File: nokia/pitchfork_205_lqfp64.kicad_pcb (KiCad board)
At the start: 2 copper layers, 108 x 41.5 mm, 85 parts, among them IC1 STM32F2XX_64LQFP, K1 CONN_3, U1 LM3670, U2 USBCONN, U3 MCP73832-2, U4 NRF24L01+, U5 MC74VHC1G66, U6 MICROSDCARD, U7 TSV912, U8 TC75W57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

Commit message: [fix] outer rings for buttons on nokia board
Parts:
- added 1Pin_12mil_VIA: VAL**, opendous:1Pin_12mil_VIA, F.Cu at (309.3, 146.4)
- added 1Pin_12mil_VIA: VAL**, opendous:1Pin_12mil_VIA, F.Cu at (278.9, 147.7)
- added 1Pin_12mil_VIA: VAL**, opendous:1Pin_12mil_VIA, F.Cu at (279.1, 144.9)
- added 1Pin_12mil_VIA: VAL**, opendous:1Pin_12mil_VIA, F.Cu at (281.6, 143.5)
- added 1Pin_12mil_VIA: VAL**, opendous:1Pin_12mil_VIA, F.Cu at (302.0, 147.6)
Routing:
- net /usb_5v: track 117.2 -> 120.9 mm
- net /usb_dm: track 66.2 -> 66.6 mm, vias 0 -> 2
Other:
- board text added: "PITCHFORK d10011"
- board text removed: "PITCHFORK d10010"

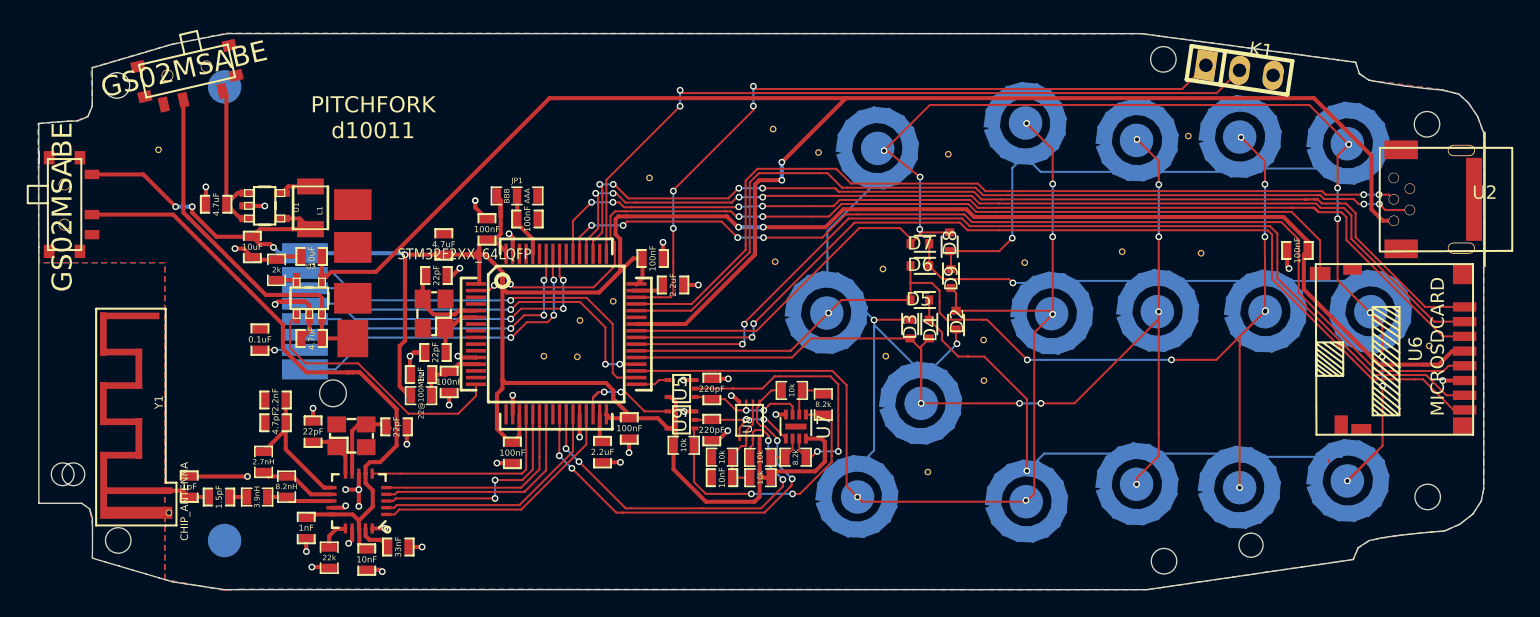
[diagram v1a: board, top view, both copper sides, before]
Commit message: [fix] lcd pinout + added R for nrf switch
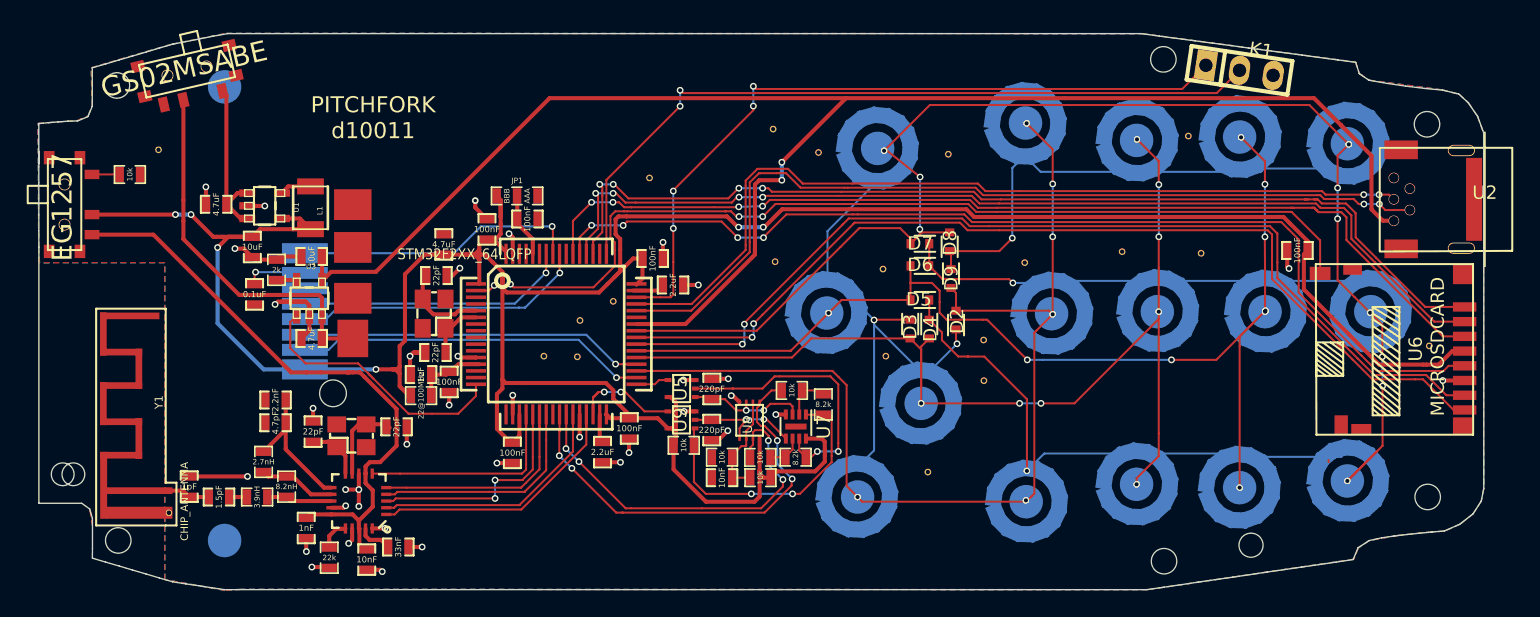
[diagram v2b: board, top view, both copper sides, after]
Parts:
- removed ? (x2): GS02MSABE, pitchforkbuttons:EG1257
- added R11: 10k, opendous:0603_Opendous, F.Cu at (245.5, 134.0)
- added SW_POWER1: GS02MSABE, pitchforkbuttons:EG1257, F.Cu at (249.7, 126.3)
- added SW_RFPWR1: EG1257, pitchforkbuttons:EG1257, F.Cu at (240.6, 136.3)
- moved C18 3.40 mm to (254.8, 143.0), turned to 270 degrees
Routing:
- net /vdd: track 219.9 -> 230.0 mm
- net /LCD_SCLK: track 30.3 -> 26.3 mm
- net /LCD_RES: track 24.9 -> 21.4 mm, vias 3 -> 1
- net /LCD_SDIN: track 29.2 -> 25.7 mm, vias 3 -> 1
- net /LCD_CS: track 23.2 -> 20.4 mm, vias 3 -> 1
- net /LCD_DC: track 24.3 -> 21.9 mm, vias 3 -> 1
- net Net-(R11-Pad2): track 0.00 -> 2.07 mm
- net Net-(C16-Pad1): track 48.3 -> 46.6 mm
- net Net-(B1-Pad15): track 3.40 -> 4.64 mm
- net /VBAT0: track 26.8 -> 27.9 mm

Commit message: [fix] corrected rf powerswitch + r11
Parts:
- added 1Pin_12mil_VIA: VAL**, opendous:1Pin_12mil_VIA, F.Cu at (305.0, 161.0)
- added 1Pin_12mil_VIA: VAL**, opendous:1Pin_12mil_VIA, F.Cu at (278.1, 161.8)
- added 1Pin_12mil_VIA: VAL**, opendous:1Pin_12mil_VIA, F.Cu at (278.1, 160.2)
- added 1Pin_12mil_VIA: VAL**, opendous:1Pin_12mil_VIA, F.Cu at (284.0, 156.9)
- added 1Pin_12mil_VIA: VAL**, opendous:1Pin_12mil_VIA, F.Cu at (251.6, 151.0)
- added 1Pin_12mil_VIA: VAL**, opendous:1Pin_12mil_VIA, F.Cu at (254.0, 153.0)
- added 1Pin_12mil_VIA: VAL**, opendous:1Pin_12mil_VIA, F.Cu at (253.9, 149.4)
- added 1Pin_12mil_VIA: VAL**, opendous:1Pin_12mil_VIA, F.Cu at (246.9, 139.5)
- moved R11 4.75 mm to (244.9, 138.8)
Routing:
- net /vdd: track 230.0 -> 231.2 mm
- net Net-(C16-Pad1): track 46.6 -> 47.2 mm

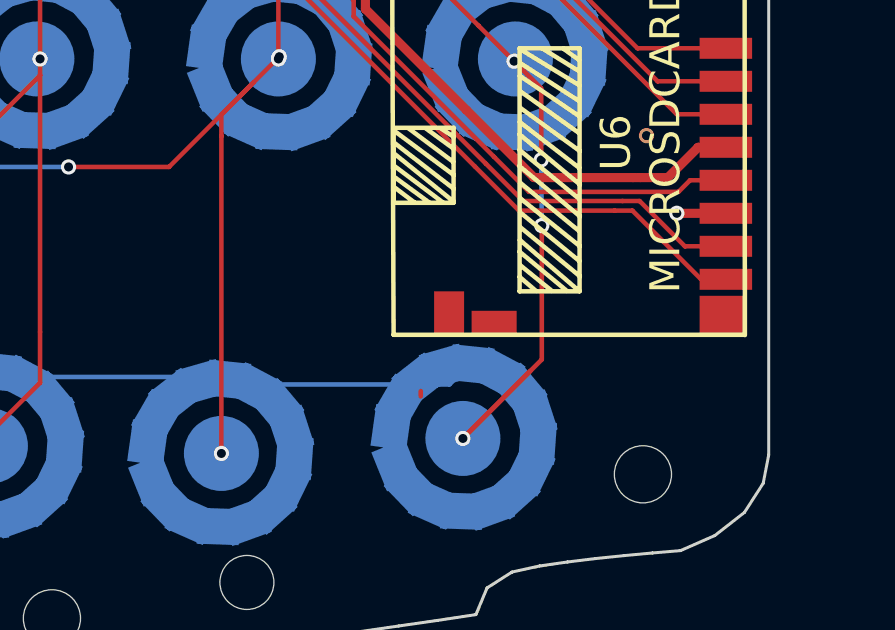
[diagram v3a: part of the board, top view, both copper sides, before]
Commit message: [fix] SD card detect GND via under pin 9 (+netlist update)
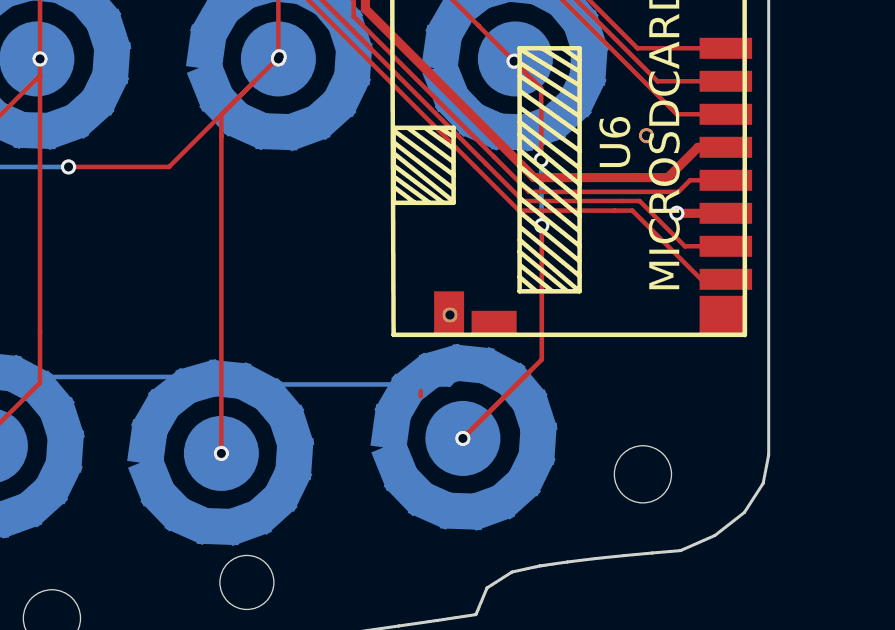
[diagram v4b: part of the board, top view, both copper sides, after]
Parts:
- added 1Pin_12mil_VIA: VAL**, opendous:1Pin_12mil_VIA, F.Cu at (336.0, 152.8)
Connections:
- U6 pad 9: Net-(U6-Pad9) -> GND
